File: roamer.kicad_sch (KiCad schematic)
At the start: 1 part

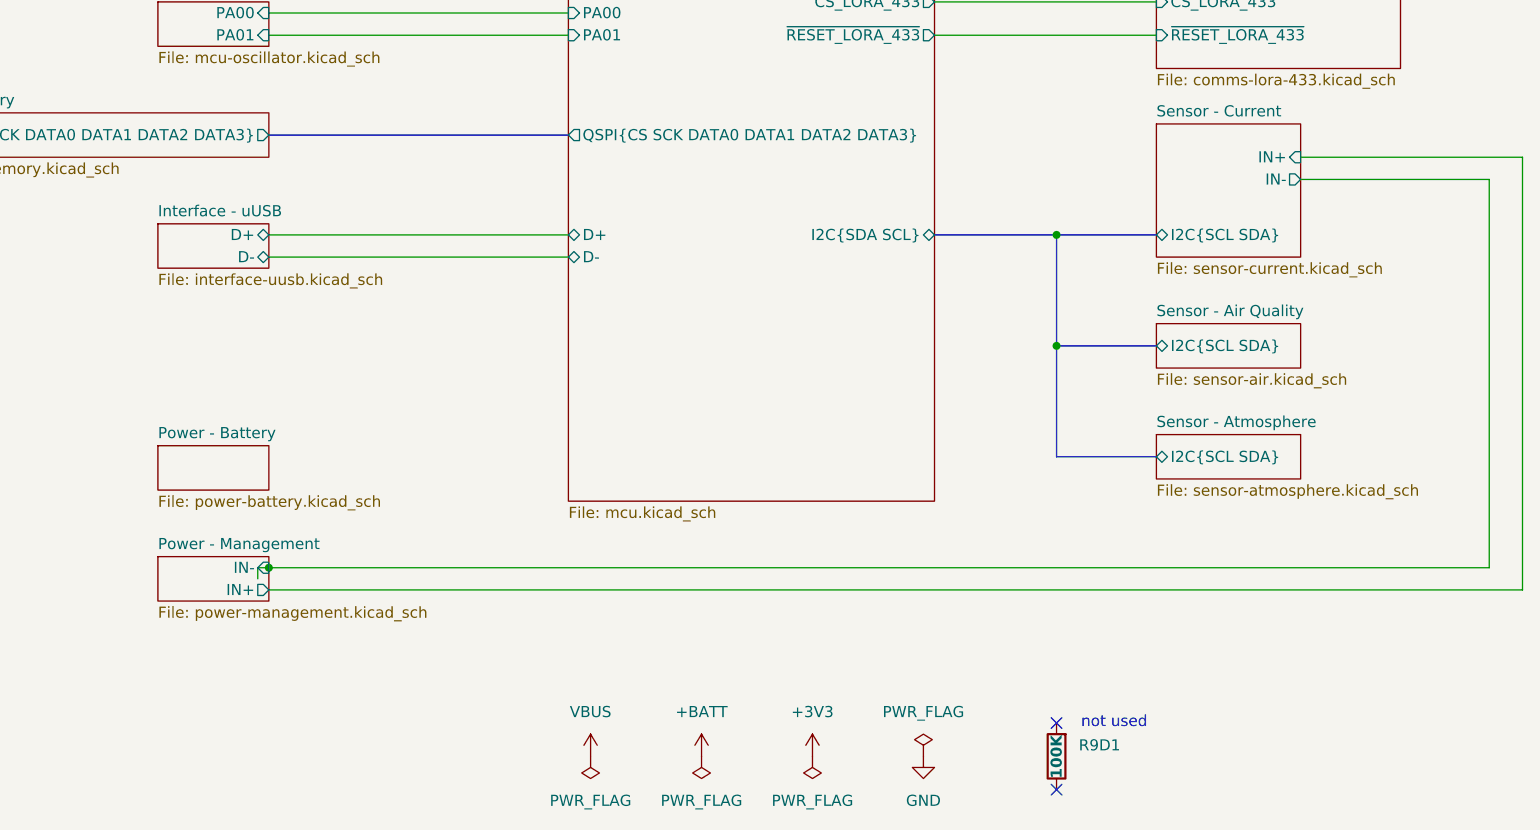
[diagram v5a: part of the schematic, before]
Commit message: Spamming 0 ohm resistors
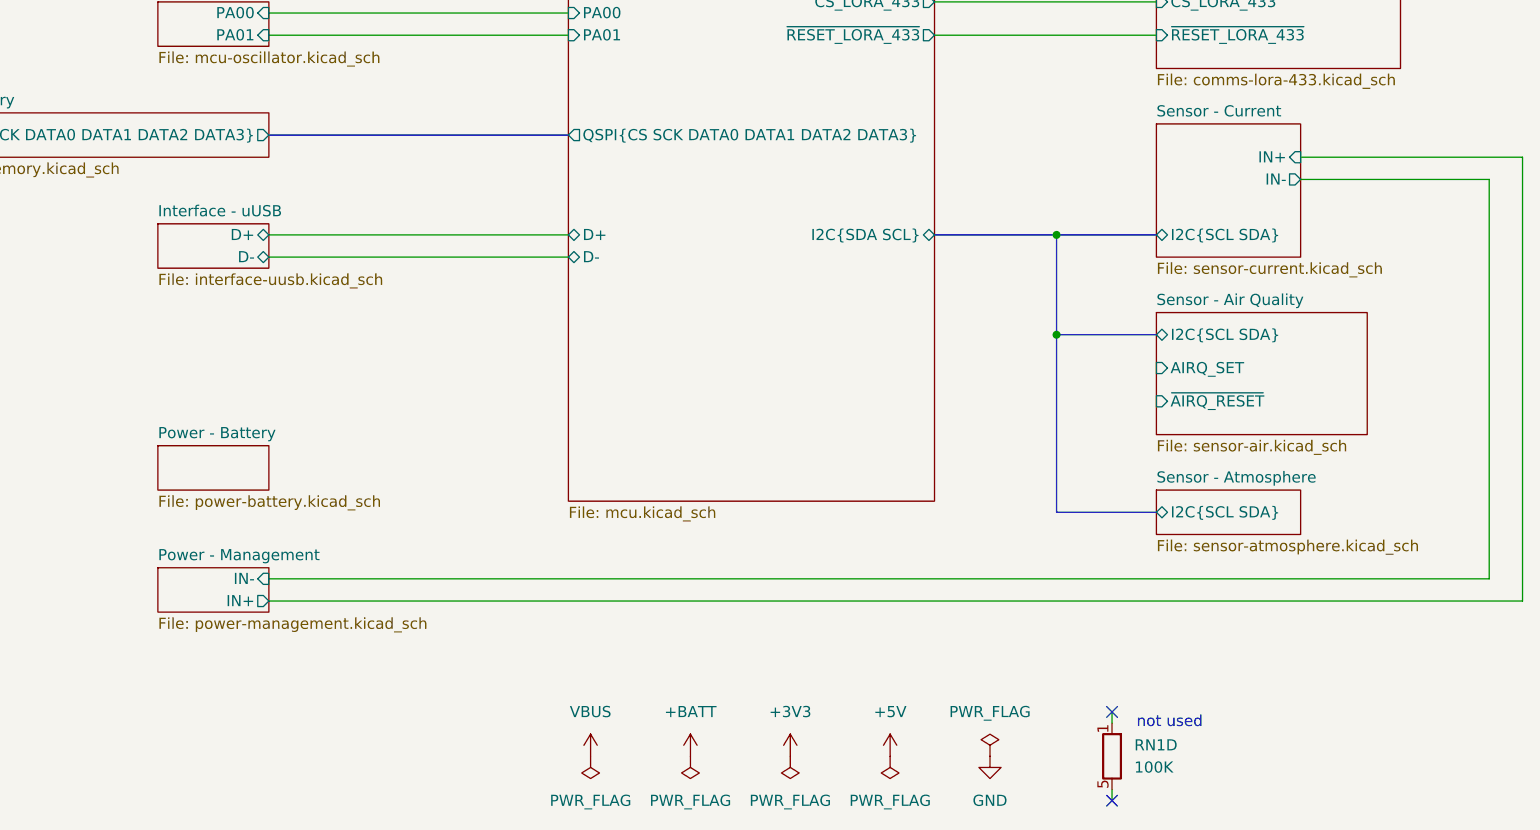
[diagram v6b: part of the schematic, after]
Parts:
- removed R9D1: 100K, Resistor_SMD:R_Array_Convex_4x1206, symbol Device:R
- added RN1: 100K, Resistor_SMD:R_Array_Convex_4x1206, symbol Device:R_Network04_Split
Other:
- sheet Sensor - Air Quality ports: added AIRQ_SET, ~{AIRQ_RESET}; removed none

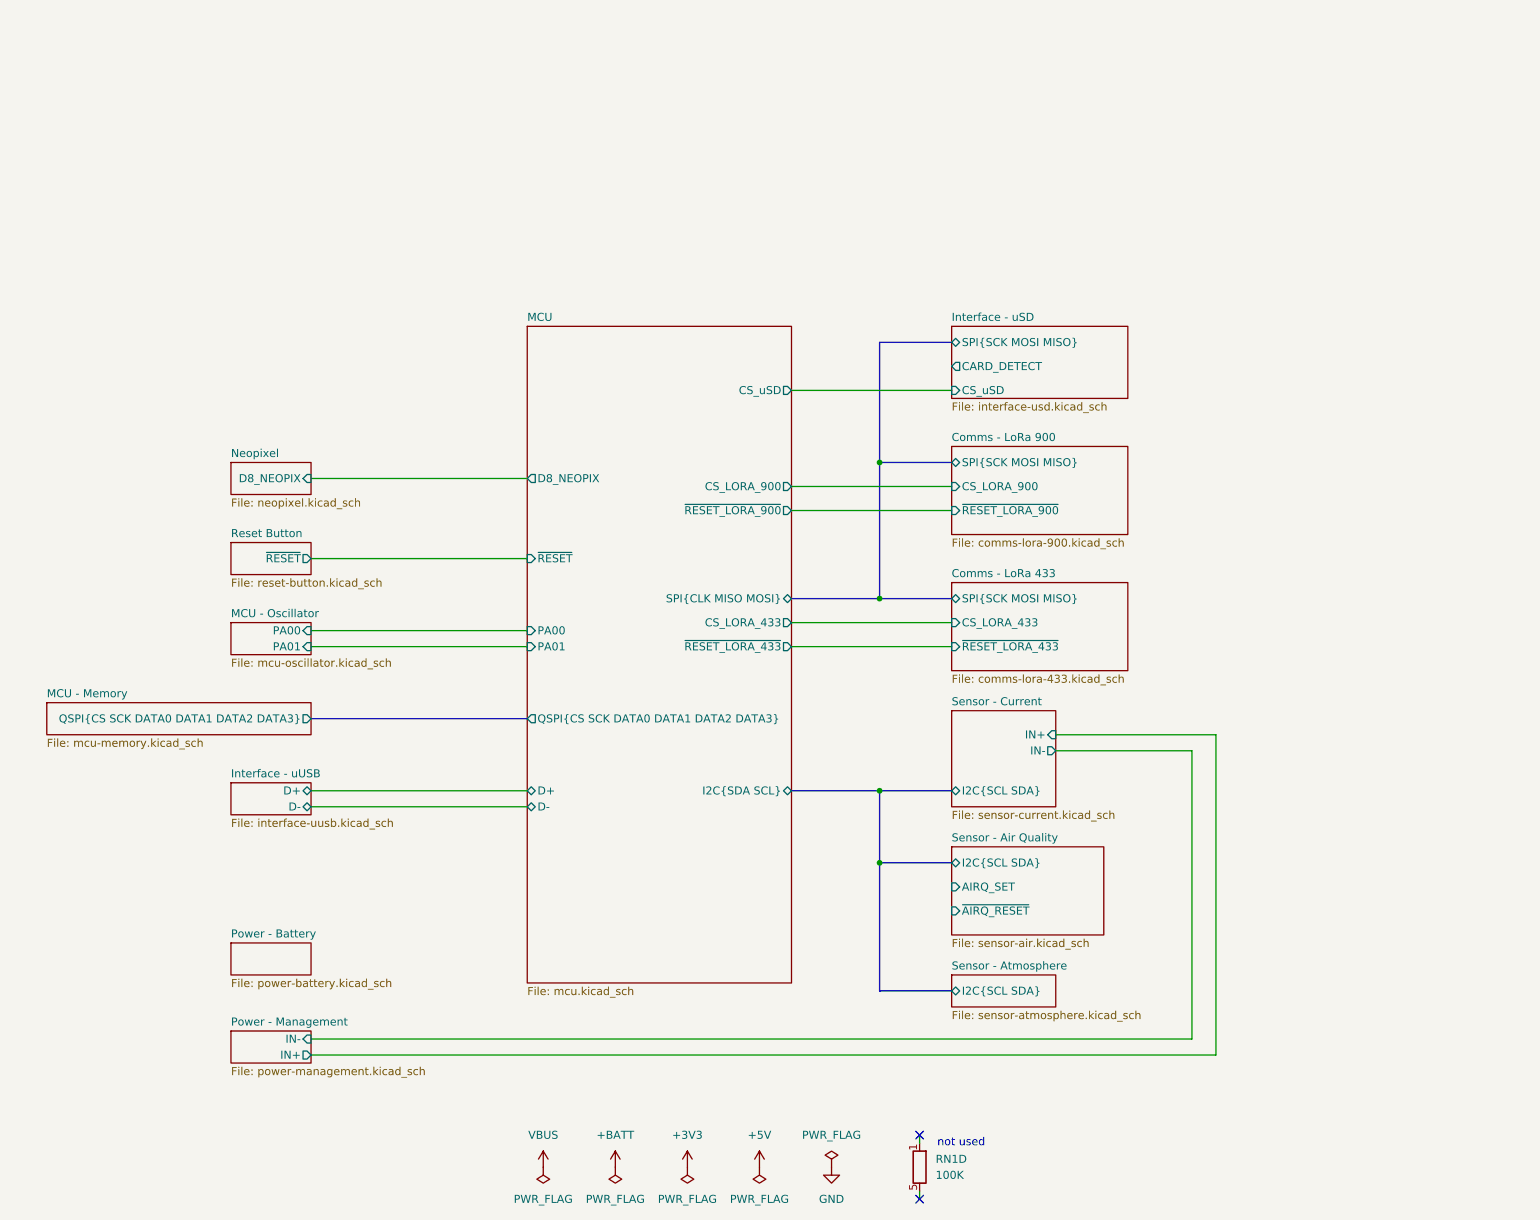
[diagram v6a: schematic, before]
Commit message: Adding more 0 ohm resistors and pullups for I2C lines
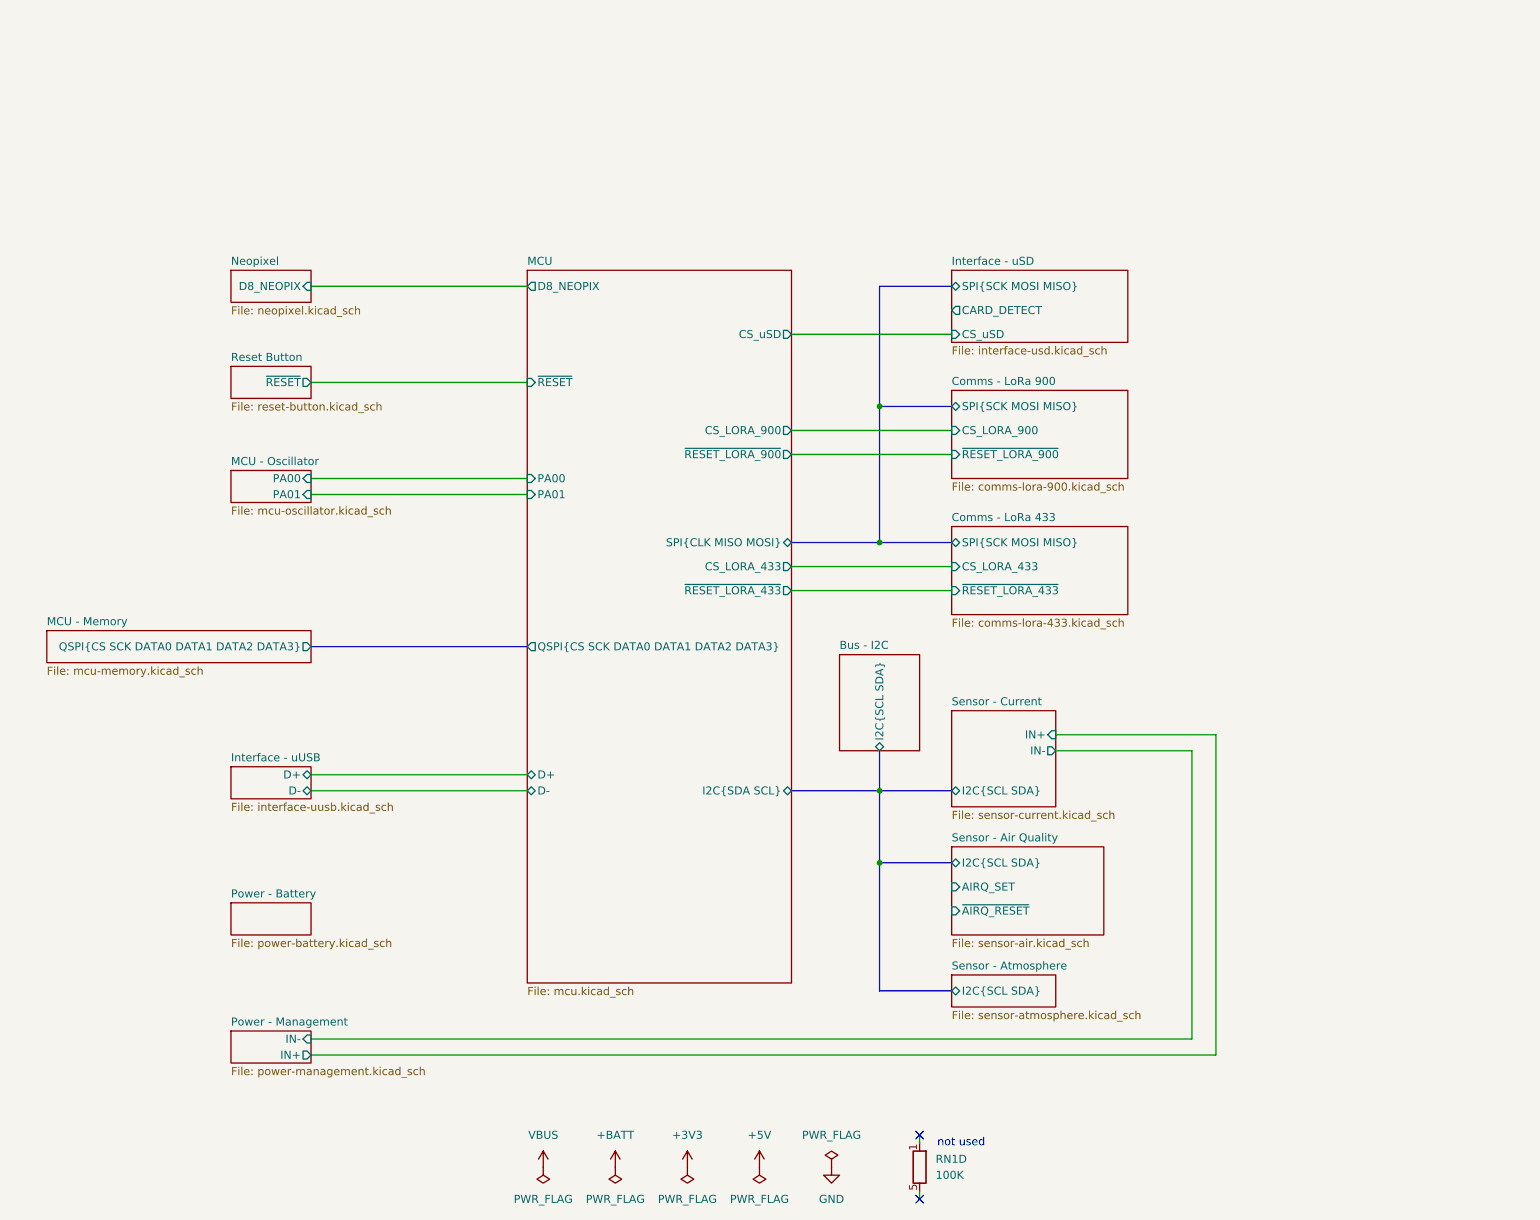
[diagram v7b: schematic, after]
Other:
- added sheet Bus - I2C (bus-i2c.kicad_sch)

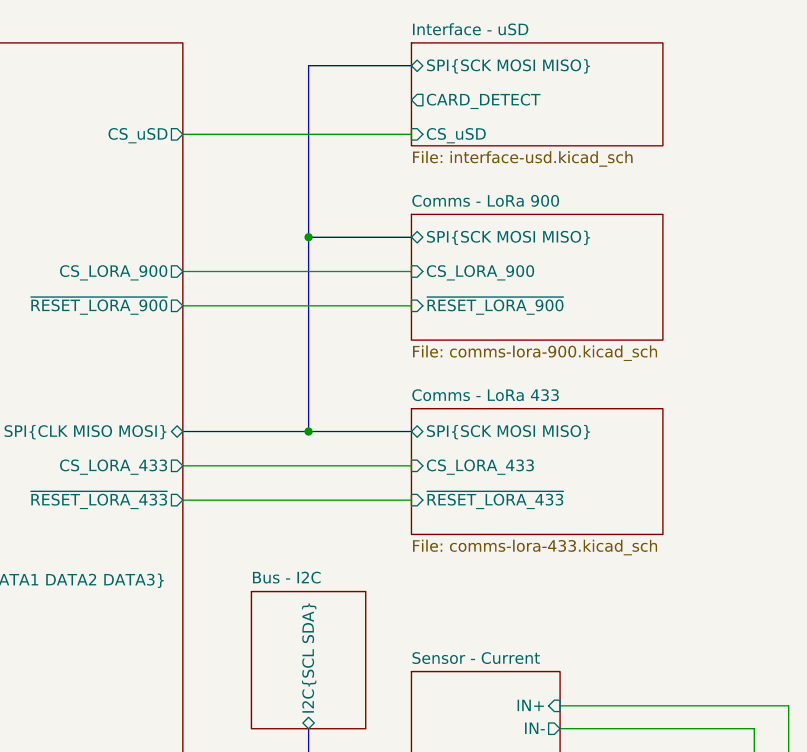
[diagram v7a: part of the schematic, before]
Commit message: Adding diodes for Air Quality Sensor SET and RESET pins
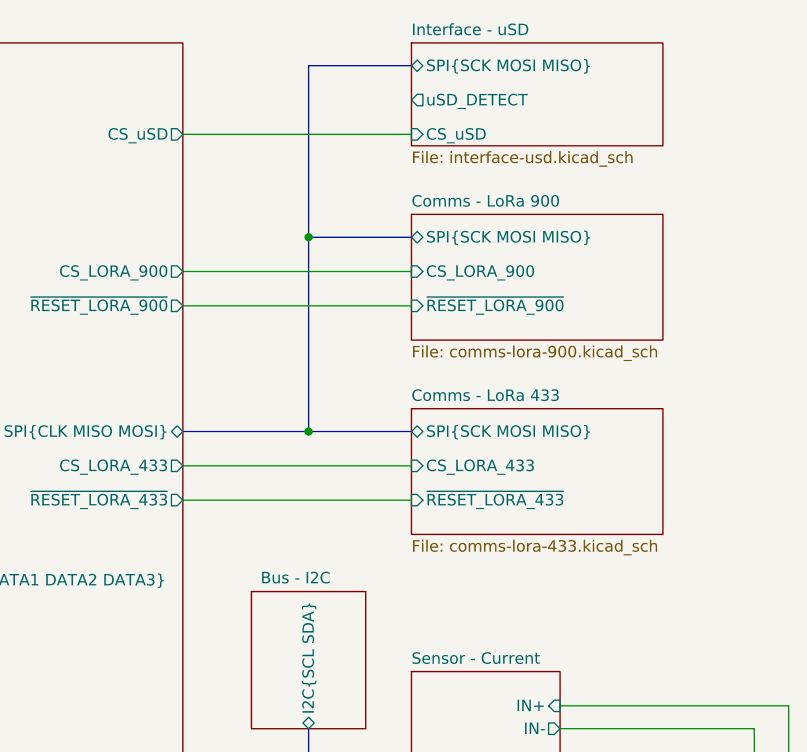
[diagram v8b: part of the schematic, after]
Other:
- sheet Interface - uSD ports: added uSD_DETECT; removed CARD_DETECT
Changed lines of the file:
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@@
-			)
-		)
-		(pin "CARD_DETECT" output
-			(at 252.73 74.93 180)
-			(effects
-				(font
-					(size 1.27 1.27)
-				)
-				(justify left)
 			)
 		)
@@
 		(pin "CS_uSD" input
 			(at 252.73 78.74 180)
+			(effects
+				(font
+					(size 1.27 1.27)
+				)
+				(justify left)
+			)
+		)
+		(pin "uSD_DETECT" output
+			(at 252.73 74.93 180)
 			(effects
 				(font
@@
 		)
 		(property "Sheetname" "Bus - I2C"
-			(at 234.95 128.778 0)
-			(effects
-				(font
+			(at 235.966 128.778 0)
+			(effects
+				(font
